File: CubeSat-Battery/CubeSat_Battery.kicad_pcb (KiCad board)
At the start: 2 copper layers, 92 x 92 mm, 8 parts, among them J1 Conn_01x02_Pin, J6 Screw_Terminal_01x02, U1 BatteryPack

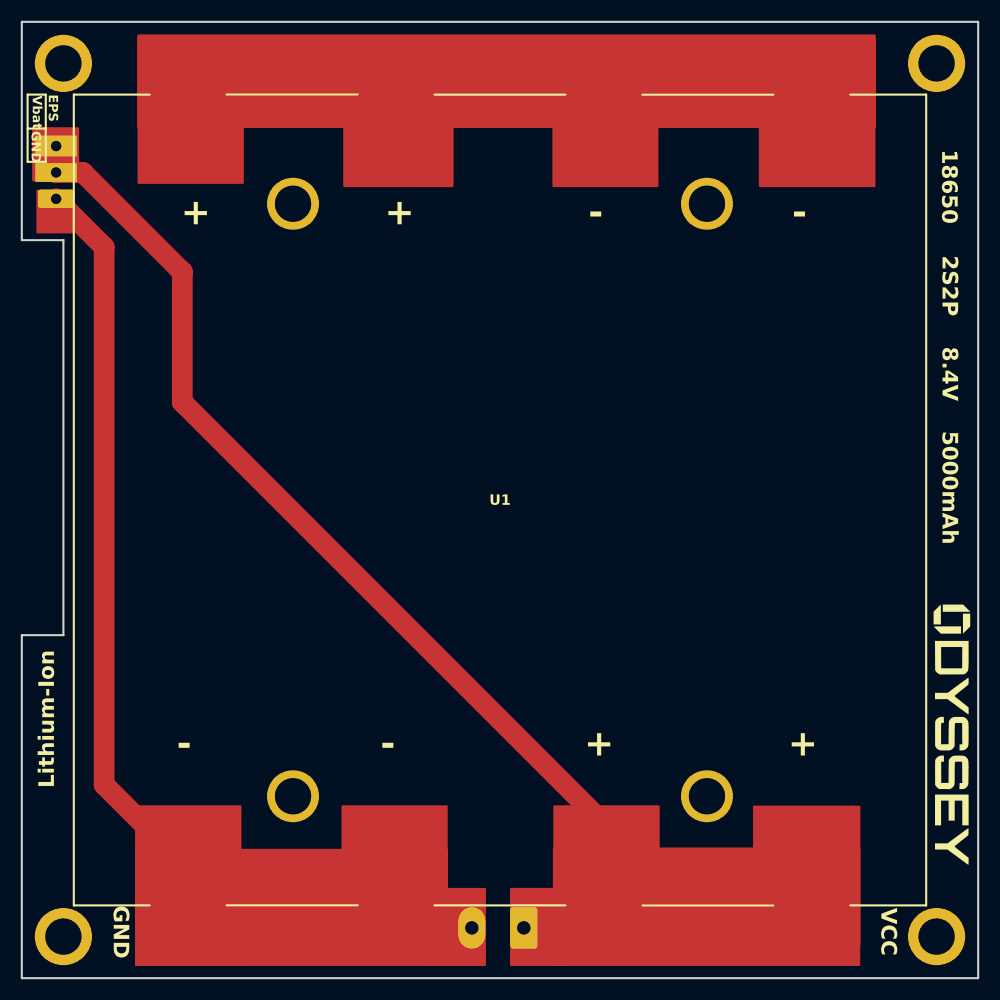
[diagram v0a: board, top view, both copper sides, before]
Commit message: new Main and EPS PCBs, all previous problems corrected, final version
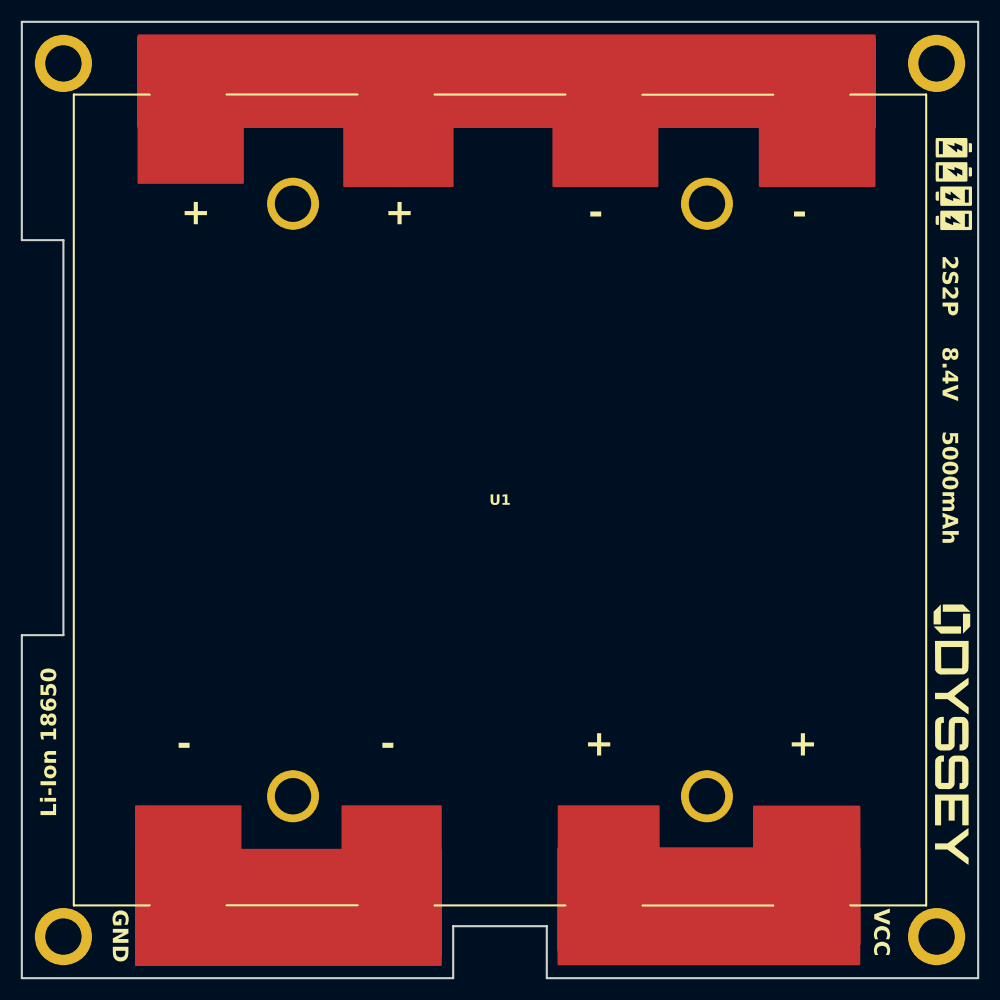
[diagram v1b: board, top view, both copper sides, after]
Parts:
- removed J1: Conn_01x02_Pin, Connector_JST:JST_EH_B2B-EH-A_1x02_P2.50mm_Vertical
- removed J6: Screw_Terminal_01x02, TerminalBlock_Phoenix:TerminalBlock_Phoenix_MKDS-1,5-2_1x02_P5.00mm_Horizontal
- added G***: LOGO, Logos:Battery_Symbol2, F.Cu at (89.7, -77.6)
- added G***: LOGO, Logos:Battery_Symbol2, F.Cu at (89.7, -72.9)
- added G***: LOGO, Logos:Battery_Symbol2, F.Cu at (89.7, -79.9)
- added G***: LOGO, Logos:Battery_Symbol2, F.Cu at (89.7, -75.2)
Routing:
- net Vbat_8.4V: track 99.4 -> 0.48 mm
- net GND: track 76.2 -> 0.48 mm
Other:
- outline, holes or cut-outs redrawn
- board text added: "Li-Ion 18650"
- board text removed: "18650"
- board text removed: "EPS"
- board text removed: "Lithium-Ion"
- board text removed: "Vbat"
